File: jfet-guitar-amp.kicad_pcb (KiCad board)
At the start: 2 copper layers, 78 x 21 mm, 48 parts, among them J1 JST_XH_2, J2 JST_XH_2, J3 JST_XH_3, Q1 J201, Q2 J201, Q3 J201, U1 4580

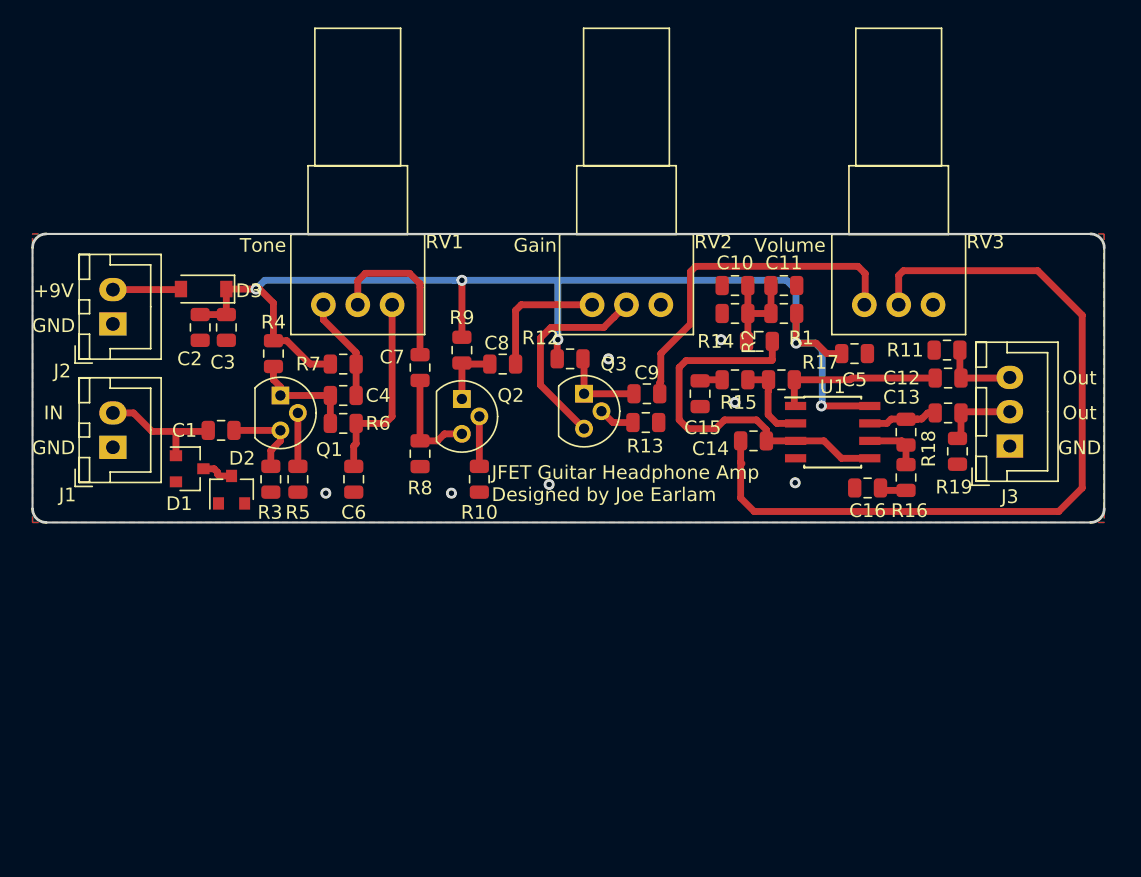
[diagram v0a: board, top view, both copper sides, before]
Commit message: changes to component footprints, new layout WIP
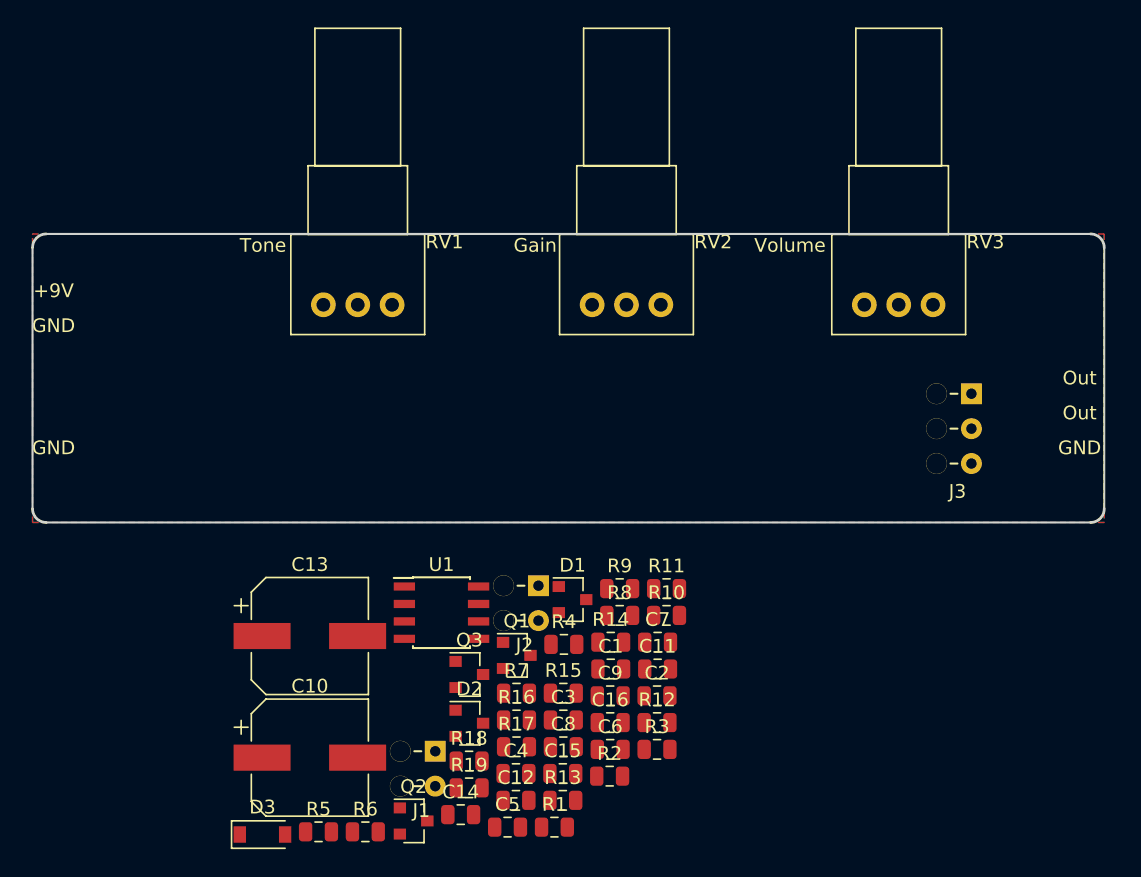
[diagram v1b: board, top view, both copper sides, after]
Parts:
- C10, C13: value 10u -> 470u; footprint Capacitor_SMD:C_0805_2012Metric -> Capacitor_SMD:CP_Elec_8x6.9
- C12: value 10u -> 220p
- C14: value 470n -> 10u
- J1, J2: footprint Connector_JST:JST_XH_B02B-XH-A_1x02_P2.50mm_Vertical -> Footprints:wire_strainrelief_2
- J3: footprint Connector_JST:JST_XH_B03B-XH-A_1x03_P2.50mm_Vertical -> Footprints:wire_strainrelief_3
- Q1, Q2, Q3: footprint Package_TO_SOT_THT:TO-92 -> Package_TO_SOT_SMD:SOT-23
- R11: value 100K -> 33K
- R14: value 47K -> 120R
- R15, R16: value 15K -> 50K
- R19: value 100K -> 120R
- moved C13 49.2 mm to (84.2, 113.3)
- moved C10 46.2 mm to (84.2, 122.1)
- moved C12 44.0 mm to (99.2, 125.2)
- moved R19 43.2 mm to (95.8, 124.3), turned to 0 degrees
- moved C5 42.7 mm to (98.6, 127.2), turned to 0 degrees
- moved C2 42.7 mm to (109.5, 117.6), turned to 0 degrees
- moved R1 40.9 mm to (102.0, 127.2), turned to 0 degrees
- moved D3 39.9 mm to (80.7, 127.7), turned to 0 degrees
- moved R18 39.8 mm to (95.8, 122.4), turned to 0 degrees
- moved C3 37.7 mm to (102.6, 119.4), turned to 0 degrees
- moved J2 37.0 mm to (100.8, 110.9), turned to 0 degrees
- moved R2 34.9 mm to (106.0, 123.5), turned to 0 degrees
- moved C14 34.6 mm to (95.2, 126.3), turned to 0 degrees
- moved R3 34.3 mm to (109.5, 121.5), turned to 0 degrees
- moved R16 33.4 mm to (99.2, 119.4), turned to 0 degrees
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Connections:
- C11 pad 1: GND -> /V_Gnd
- C11 pad 2: /V_Gnd -> GND
- C12 pad 1: Net-(C12-Pad1) -> GND
- C13 pad 1: Net-(C13-Pad1) -> /V_Gnd
- C13 pad 2: Net-(C13-Pad2) -> +9V
- C14 pad 2: Net-(C14-Pad2) -> GND
- J3 pad 1: GND -> /V_Gnd
- J3 pad 2: Net-(C13-Pad2) -> Net-(J3-Pad2)
- J3 pad 3: Net-(C12-Pad2) -> Net-(J3-Pad3)
- Q1 pad 1: Net-(C4-Pad2) -> Net-(C8-Pad2)
- Q1 pad 3: Net-(C1-Pad1) -> Net-(C12-Pad2)
- Q2 pad 1: Net-(C8-Pad2) -> Net-(C4-Pad2)
- Q2 pad 3: Net-(C7-Pad1) -> Net-(Q2-Pad3)
- Q3 pad 2: Net-(Q3-Pad2) -> Net-(C14-Pad1)
- Q3 pad 3: Net-(Q3-Pad3) -> Net-(C7-Pad1)
- R10 pad 1: Net-(Q2-Pad2) -> Net-(C14-Pad1)
- R11 pad 1: GND -> Net-(C12-Pad2)
- R11 pad 2: Net-(C12-Pad2) -> Net-(C1-Pad1)
- R12 pad 1: Net-(C9-Pad2) -> Net-(C4-Pad2)
- R13 pad 1: Net-(Q3-Pad2) -> Net-(Q2-Pad2)
- R14 pad 1: /V_Gnd -> Net-(R14-Pad1)
- R14 pad 2: Net-(C14-Pad1) -> Net-(J3-Pad3)
- R17 pad 1: Net-(C12-Pad1) -> Net-(R14-Pad1)
- R18 pad 1: Net-(C13-Pad1) -> Net-(R18-Pad1)
- R19 pad 1: GND -> Net-(J3-Pad2)
- R19 pad 2: Net-(C13-Pad2) -> Net-(R18-Pad1)
- R4 pad 1: Net-(C4-Pad2) -> Net-(C8-Pad2)
- R9 pad 1: Net-(C8-Pad2) -> Net-(C9-Pad2)
- RV2 pad 2: Net-(Q3-Pad3) -> Net-(Q2-Pad3)
- RV3 pad 1: GND -> /V_Gnd
- RV3 pad 2: Net-(C14-Pad2) -> Net-(RV3-Pad2)
- U1 pad 1: Net-(C12-Pad1) -> Net-(R14-Pad1)
- U1 pad 3: Net-(C14-Pad1) -> Net-(RV3-Pad2)
- U1 pad 5: Net-(C14-Pad1) -> Net-(RV3-Pad2)
- U1 pad 7: Net-(C13-Pad1) -> Net-(R18-Pad1)
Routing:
- net +9V: track 84.6 -> 0.00 mm, vias 5 -> 0
- net Net-(C14-Pad2): track 60.0 -> 0.00 mm
- net Net-(C14-Pad1): track 28.3 -> 0.00 mm
- net Net-(C9-Pad1): track 25.1 -> 0.00 mm
- net Net-(Q3-Pad3): track 15.2 -> 0.00 mm
- net Net-(C6-Pad2): track 14.2 -> 0.00 mm
- net Net-(C12-Pad1): track 12.3 -> 0.00 mm
- net Net-(C7-Pad2): track 12.0 -> 0.00 mm
- net Net-(C8-Pad1): track 9.59 -> 0.00 mm
- net Net-(C1-Pad2): track 9.30 -> 0.00 mm
- net Net-(C4-Pad2): track 7.99 -> 0.00 mm
- net /V_Gnd: track 7.82 -> 0.00 mm
- net Net-(C7-Pad1): track 7.65 -> 0.00 mm
- net Net-(C4-Pad1): track 7.34 -> 0.00 mm
- net Net-(C1-Pad1): track 6.40 -> 0.00 mm
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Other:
- board text removed: "IN"
- board text removed: "JFET Guitar Headphone Amp Designed by Joe Earlam"

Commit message: PCB updated
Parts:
- added R21: 4K7, Resistor_SMD:R_0805_2012Metric, F.Cu at (98.2, 95.2)
- added R22: 4K7, Resistor_SMD:R_0805_2012Metric, F.Cu at (101.6, 95.2)
- added U2: TSX9291, Package_TO_SOT_SMD:SOT-23-5, F.Cu at (86.4, 101.9)
- C10: value 470u -> 100n; footprint Capacitor_SMD:CP_Elec_8x6.9 -> Capacitor_SMD:C_0805_2012Metric
- C11: value 100n -> 470u; footprint Capacitor_SMD:C_0805_2012Metric -> Capacitor_SMD:C_Elec_8x6.2
- C13: footprint Capacitor_SMD:CP_Elec_8x6.9 -> Capacitor_SMD:C_Elec_8x6.2
- J1, J2: value JST_XH_2 -> Conn_2
- J3: value JST_XH_3 -> Conn_3
- R1, R2: value 47K -> 100K
- R15, R16: value 50K -> 33K
- moved R19 45.0 mm to (131.7, 97.3), turned to 180 degrees
- moved C12 44.8 mm to (70.0, 91.3)
- moved R3 44.3 mm to (77.1, 91.3)
- moved C5 42.3 mm to (132.8, 102.4), turned to 180 degrees
- moved C1 41.9 mm to (73.7, 89.2), turned to 180 degrees
- moved J1 41.6 mm to (70.9, 87.9)
- moved C14 41.5 mm to (115.6, 90.2)
- moved R17 41.0 mm to (128.5, 92.6), turned to 180 degrees
- moved R11 41.0 mm to (73.5, 91.3)
- moved C2 38.5 mm to (75.6, 99.4)
- moved D1 38.3 mm to (73.8, 86.2), turned to 90 degrees
- moved D2 38.1 mm to (77.5, 86.2), turned to 90 degrees
- moved R18 36.7 mm to (126.6, 102.4), turned to 180 degrees
- moved C8 36.5 mm to (77.1, 95.2), turned to 180 degrees
- moved U1 36.0 mm to (126.9, 97.4), turned to 270 degrees
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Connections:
- C10 pad 1: GND -> +9V
- C10 pad 2: /V_Gnd -> GND
- C11 pad 2: GND -> +9V
- C13 pad 1: /V_Gnd -> GND
- C13 pad 2: +9V -> /V_Gnd
- R1 pad 1: +9V -> Net-(R1-Pad1)
- R1 pad 2: /V_Gnd -> +9V
- R2 pad 1: /V_Gnd -> GND
- R2 pad 2: GND -> Net-(R1-Pad1)
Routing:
- net +9V: track 0.00 -> 113.1 mm, vias 0 -> 3
- net /V_Gnd: track 0.00 -> 92.5 mm, vias 0 -> 1
- net Net-(C6-Pad2): track 0.00 -> 27.3 mm, vias 0 -> 1
- net Net-(C4-Pad1): track 0.00 -> 16.2 mm
- net Net-(RV3-Pad2): track 0.00 -> 13.8 mm, vias 0 -> 1
- net Net-(C9-Pad1): track 0.00 -> 10.3 mm
- net Net-(C8-Pad1): track 0.00 -> 9.11 mm
- net Net-(R18-Pad1): track 0.00 -> 7.89 mm
- net Net-(R15-Pad1): track 0.00 -> 6.38 mm
- net Net-(C4-Pad2): track 0.00 -> 5.31 mm
- net Net-(R14-Pad1): track 0.00 -> 5.11 mm
- net Net-(R16-Pad1): track 0.00 -> 5.03 mm
- net Net-(C7-Pad2): track 0.00 -> 4.68 mm
- net Net-(C12-Pad2): track 0.00 -> 4.63 mm
- net Net-(Q2-Pad3): track 0.00 -> 4.39 mm
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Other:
- board text added: "IN"

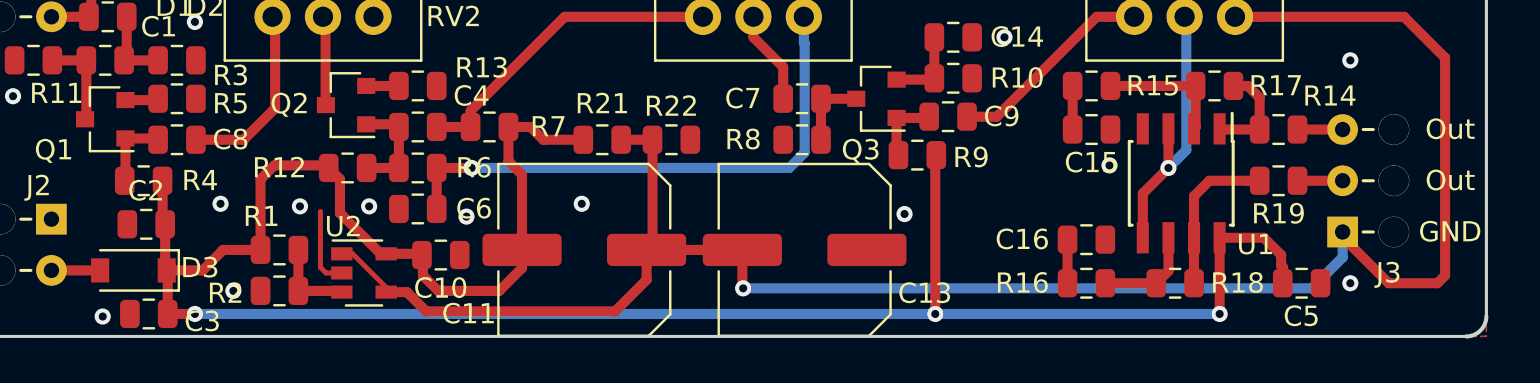
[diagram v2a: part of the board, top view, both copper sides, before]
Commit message: minor component value changes
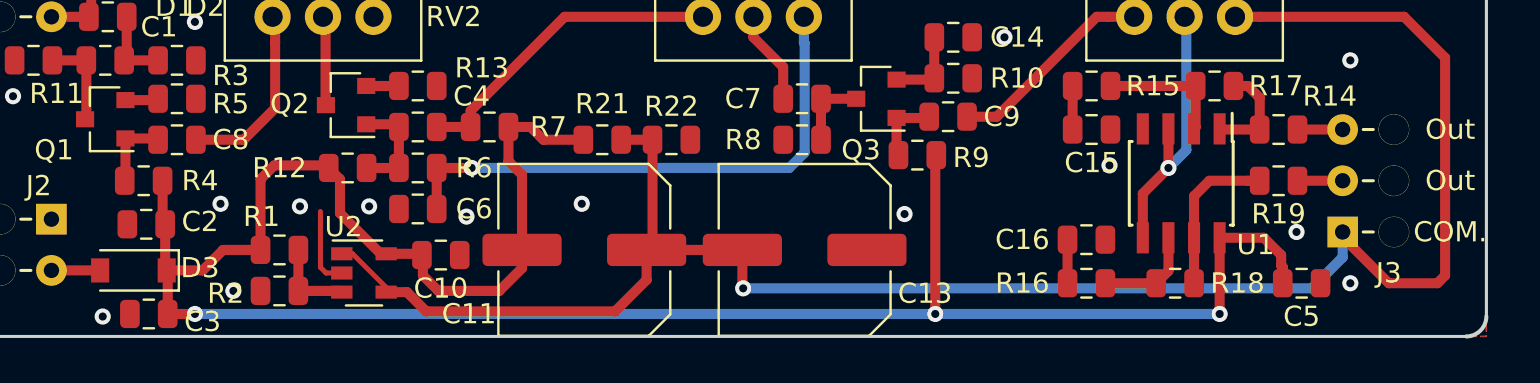
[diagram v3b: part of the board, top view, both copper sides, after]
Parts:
- C14, C15, C16, C2, C3: value 10u -> 4u7
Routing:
- net GND: vias 14 -> 15
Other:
- board text added: "COM."
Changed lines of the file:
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@@
-(kicad_pcb (version 20171130) (host pcbnew 5.0.2-bee76a0~70~ubuntu18.04.1)
+(kicad_pcb (version 20171130) (host pcbnew "(5.0.0)")
   (general
     (thickness 1.6)
     (drawings 18)
-    (tracks 173)
+    (tracks 174)
     (zones 0)
     (modules 51)
@@
   )
   (setup
-    (last_trace_width 0.5)
+    (last_trace_width 0.25)
     (user_trace_width 0.5)
     (trace_clearance 0.2)
@@
       (effects (font (size 1 1) (thickness 0.15)))
     )
-    (fp_text value 10u (at 0 1.65 180) (layer F.Fab)
+    (fp_text value 4u7 (at 0 1.65 180) (layer F.Fab)
       (effects (font (size 1 1) (thickness 0.15)))
     )
@@
       (effects (font (size 1 1) (thickness 0.15)))
     )
-    (fp_text value 10u (at 0 1.65 180) (layer F.Fab)
+    (fp_text value 4u7 (at 0 1.65 180) (layer F.Fab)
       (effects (font (size 1 1) (thickness 0.15)))
     )
@@
       (effects (font (size 1 1) (thickness 0.15)))
     )
-    (fp_text value 10u (at 0 1.65) (layer F.Fab)
+    (fp_text value 4u7 (at 0 1.65) (layer F.Fab)
       (effects (font (size 1 1) (thickness 0.15)))
     )
@@
     (tags capacitor)
     (attr smd)
-    (fp_text reference C2 (at 0 -1.65) (layer F.SilkS)
-      (effects (font (size 1 1) (thickness 0.15)))
-    )
-    (fp_text value 10u (at 0 1.65) (layer F.Fab)
+    (fp_text reference C2 (at 2.667 -0.127) (layer F.SilkS)
+      (effects (font (size 1 1) (thickness 0.15)))
+    )
+    (fp_text value 4u7 (at 0 1.65) (layer F.Fab)
       (effects (font (size 1 1) (thickness 0.15)))
     )
@@
       (effects (font (size 1 1) (thickness 0.15)))
     )
-    (fp_text value 10u (at 0 1.65) (layer F.Fab)
+    (fp_text value 4u7 (at 0 1.65) (layer F.Fab)
       (effects (font (size 1 1) (thickness 0.15)))
     )
@@
     (effects (font (size 1 1) (thickness 0.2)))
   )
-  (gr_text GND (at 140.208 99.822) (layer F.SilkS)
+  (gr_text COM. (at 140.208 99.822) (layer F.SilkS)
     (effects (font (size 1 1) (thickness 0.2)))
   )
@@
   (segment (start 93.5205 96.3145) (end 94.1945 96.9885) (width 0.5) (layer F.Cu) (net 2))
   (segment (start 93.5205 94.615) (end 93.5205 96.3145) (width 0.5) (layer F.Cu) (net 2))
-  (segment (start 131.9045 101.562) (end 131.826 101.4835) (width 0.5) (layer F.Cu) (net 2))
-  (segment (start 131.9045 102.362) (end 131.9045 101.562) (width 0.5) (layer F.Cu) (net 2))
-  (segment (start 131.826 101.4835) (end 131.826 100.965) (width 0.5) (layer F.Cu) (net 2))
-  (segment (start 130.97 100.109) (end 128.778 100.109) (width 0.5) (layer F.Cu) (net 2))
-  (segment (start 131.826 100.965) (end 130.97 100.109) (width 0.5) (layer F.Cu) (net 2))
   (segment (start 87.188 100.904) (end 87.46 100.904) (width 0.5) (layer F.Cu) (net 2))
   (segment (start 85.168237 98.884237) (end 87.188 100.904) (width 0.5) (layer F.Cu) (net 2))
@@
   (segment (start 114.681 103.886) (end 128.778 103.886) (width 0.5) (layer B.Cu) (net 2))
   (segment (start 128.778 103.886) (end 128.778 100.109) (width 0.5) (layer F.Cu) (net 2))
+  (segment (start 131.826 100.965) (end 130.97 100.109) (width 0.5) (layer F.Cu) (net 2) (status 1000000))
+  (segment (start 130.97 100.109) (end 128.778 100.109) (width 0.5) (layer F.Cu) (net 2) (status 1000000))
+  (segment (start 131.826 101.4835) (end 131.826 100.965) (width 0.5) (layer F.Cu) (net 2) (status 1000000))
+  (segment (start 131.9045 102.362) (end 131.9045 101.562) (width 0.5) (layer F.Cu) (net 2) (status 1000000))
+  (segment (start 131.9045 101.562) (end 131.826 101.4835) (width 0.5) (layer F.Cu) (net 2) (status 1000000))
   (segment (start 114.3175 94.168) (end 114.3785 94.107) (width 0.5) (layer F.Cu) (net 3))
   (segment (start 112.76 94.168) (end 114.3175 94.168) (width 0.5) (layer F.Cu) (net 3))
@@
   (via (at 135.255 91.313) (size 0.8) (drill 0.4) (layers F.Cu B.Cu) (net 8))
   (via (at 79.248 98.425) (size 0.8) (drill 0.4) (layers F.Cu B.Cu) (net 8))
+  (via (at 132.588 99.822) (size 0.8) (drill 0.4) (layers F.Cu B.Cu) (net 8))
   (segment (start 74.5975 91.186) (end 74.4705 91.313) (width 0.5) (layer F.Cu) (net 9))
   (segment (start 74.5975 89.154) (end 74.5975 91.186) (width 0.5) (layer F.Cu) (net 9))

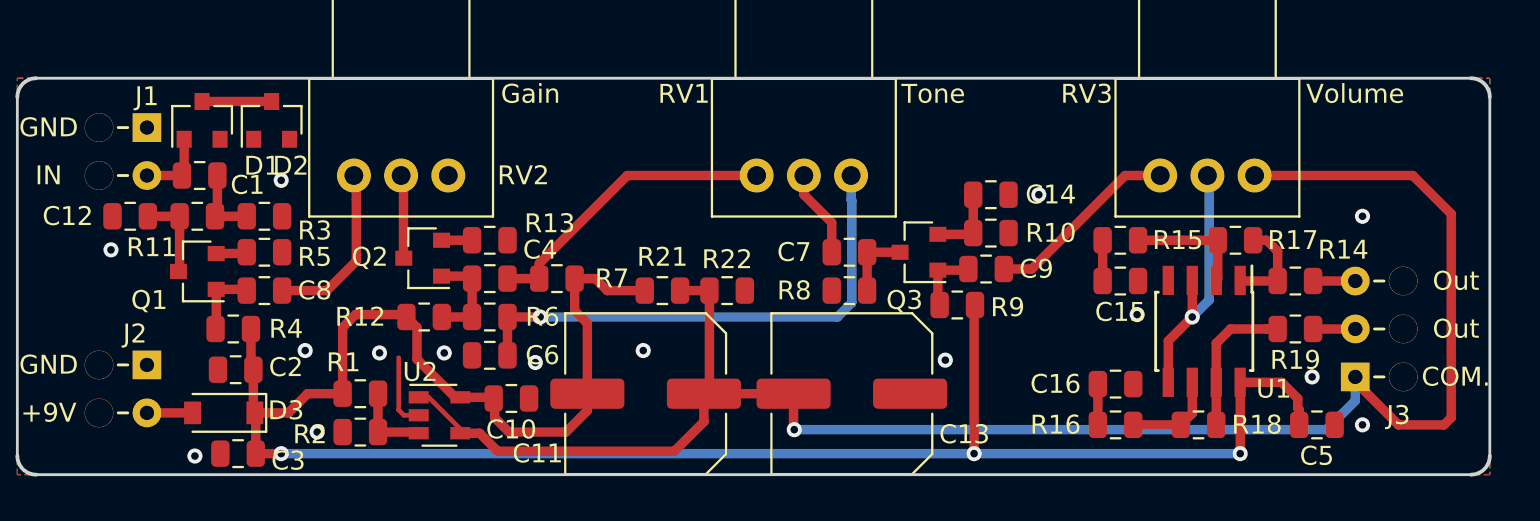
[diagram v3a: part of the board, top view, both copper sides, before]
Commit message: added PCB mount headphone socket, minor component changes
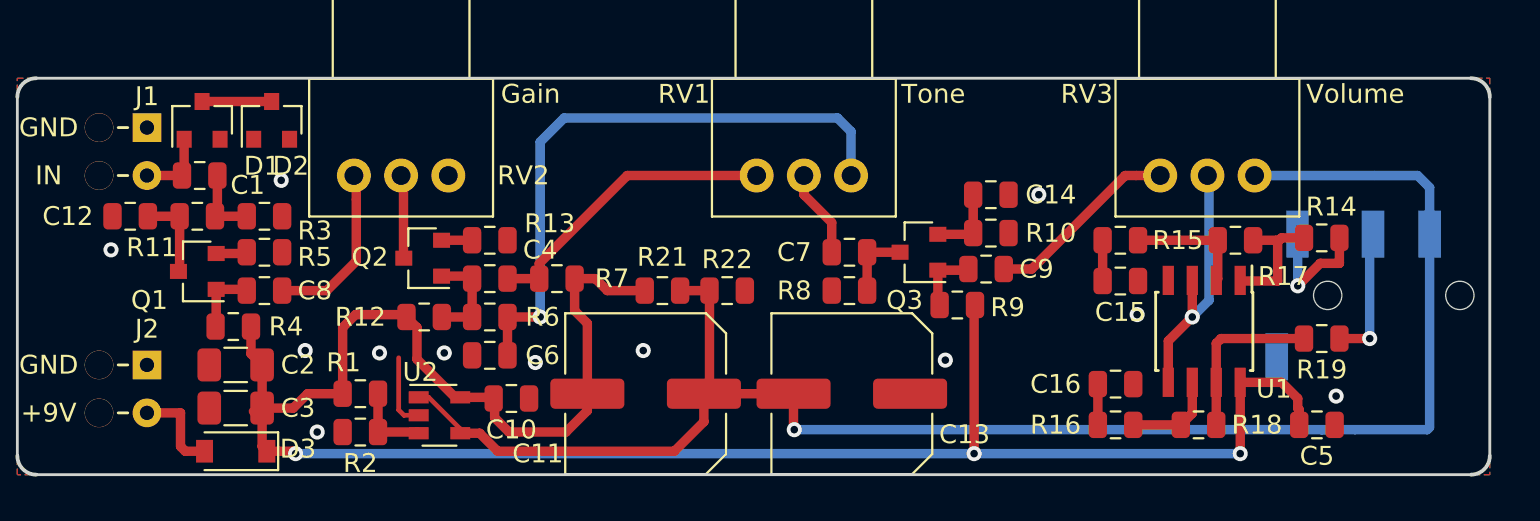
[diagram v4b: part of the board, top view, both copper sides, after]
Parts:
- C2, C3: value 4u7 -> 10u; footprint Capacitor_SMD:C_0805_2012Metric -> Capacitor_SMD:C_1206_3216Metric
- J3: value Conn_3 -> AudioJack4; footprint Footprints:wire_strainrelief_3 -> Connector_Audio:Jack_3.5mm_PJ320D_Horizontal; moved to B.Cu
- moved R14 2.68 mm to (133.1, 92.5)
- moved C3 2.42 mm to (75.6, 101.5)
- moved D3 2.13 mm to (75.6, 103.8)
- moved J3 1.93 mm to (135.6, 95.5)
- moved R19 1.49 mm to (133.1, 97.8)
- moved C2 0.25 mm to (75.6, 99.2)
- moved R4 0.13 mm to (75.4, 97.2)
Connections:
- R14 pad 2: Net-(J3-Pad3) -> Net-(J3-PadT)
- R19 pad 1: Net-(J3-Pad2) -> Net-(J3-PadR1)
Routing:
- net Net-(J3-PadR1): track 0.00 -> 7.21 mm, vias 0 -> 1
- net Net-(J3-PadT): track 0.00 -> 6.80 mm, vias 0 -> 1
- net Net-(C6-Pad2): track 27.3 -> 32.7 mm
- net /V_Gnd: track 92.5 -> 88.9 mm
- net Net-(D3-Pad2): track 2.41 -> 4.93 mm
- net Net-(J3-Pad3): track 2.24 -> 0.00 mm
- net Net-(J3-Pad2): track 2.24 -> 0.00 mm
- net Net-(R14-Pad1): track 5.11 -> 6.89 mm
- net Net-(R18-Pad1): track 7.89 -> 9.07 mm
- net GND: vias 15 -> 12
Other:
- board text added: "JFET guitar headphone amp Designed by Joe Earlam Rev2"
- board text removed: "COM."
- board text removed: "Out"
